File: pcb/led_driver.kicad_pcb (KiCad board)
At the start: 2 copper layers, 99.8 x 73.5 mm, 60 parts, among them J1 48V IN, J2 LED, J3 12V IN, J4 INTERLOCK, Q1 IRF540N, SW3 ARM, U1 TC4427xOA, U2 74HC74, U3 74HC08, U4 LM393

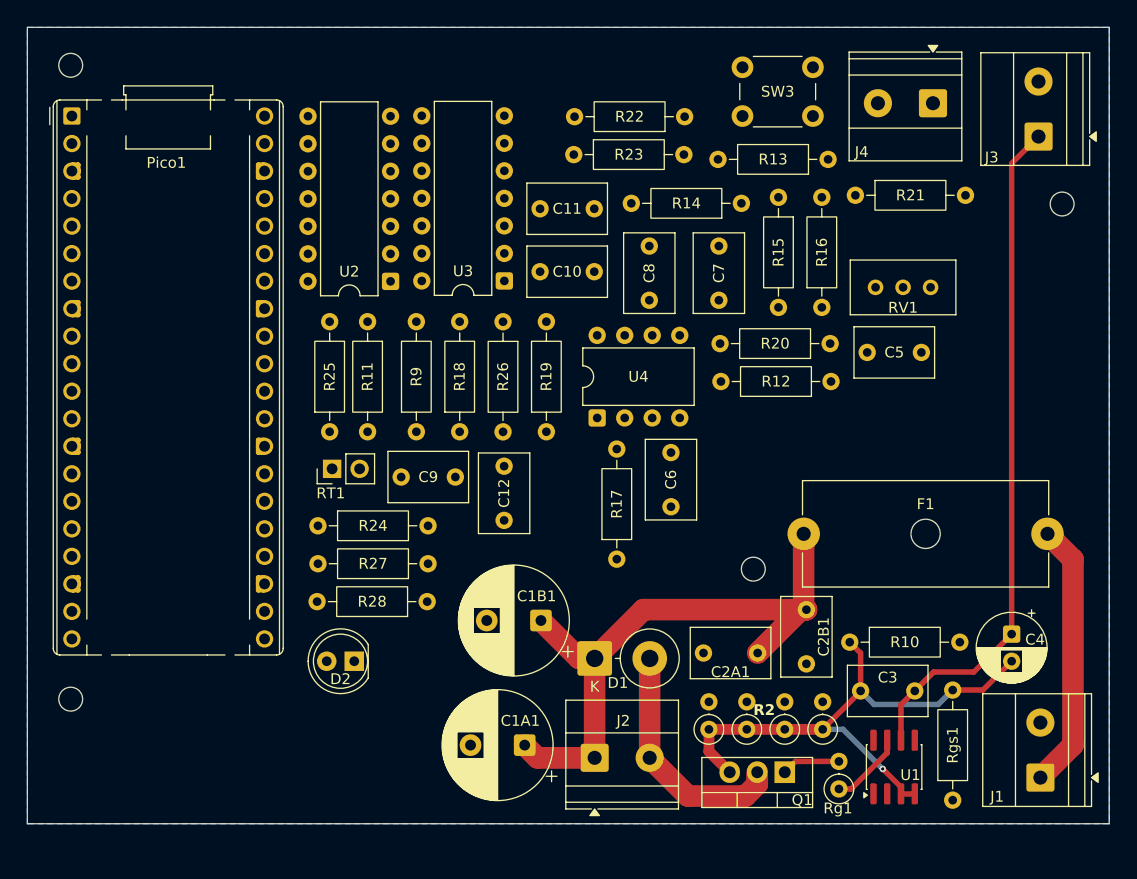
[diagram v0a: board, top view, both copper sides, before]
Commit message: Initial routing for LED driver
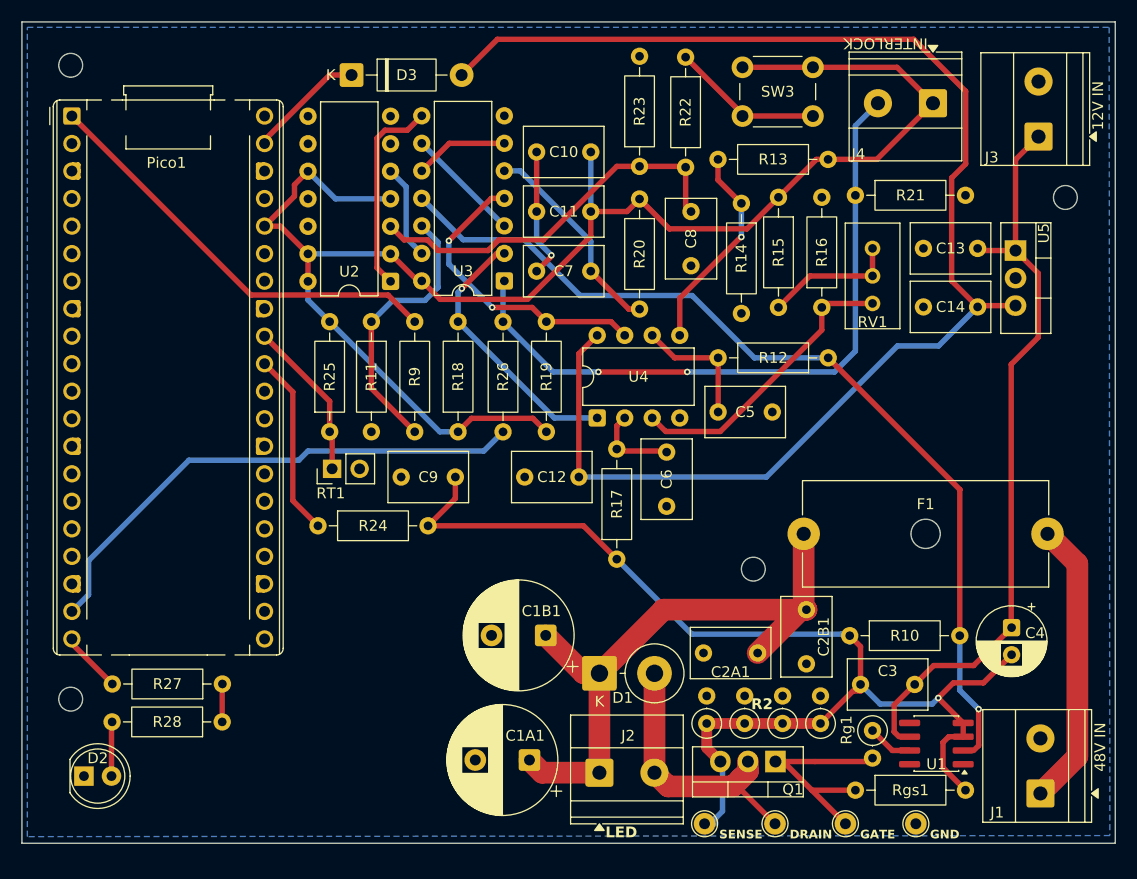
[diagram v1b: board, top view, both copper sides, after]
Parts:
- added C13: 100nF, Capacitor_THT:C_Rect_L7.2mm_W4.5mm_P5.00mm_FKS2_FKP2_MKS2_MKP2, F.Cu at (184.2, 80.4)
- added C14: 100nF, Capacitor_THT:C_Rect_L7.2mm_W4.5mm_P5.00mm_FKS2_FKP2_MKS2_MKP2, F.Cu at (179.2, 85.8)
- added D3: 1N5819, Diode_THT:D_DO-41_SOD81_P10.16mm_Horizontal, F.Cu at (126.4, 64.4)
- added TP1: TestPoint, TestPoint:TestPoint_THTPad_D2.0mm_Drill1.0mm, F.Cu at (172.0, 133.5)
- added TP2: TestPoint, TestPoint:TestPoint_THTPad_D2.0mm_Drill1.0mm, F.Cu at (165.5, 133.5)
- added TP3: TestPoint, TestPoint:TestPoint_THTPad_D2.0mm_Drill1.0mm, F.Cu at (159.0, 133.5)
- added TP4: TestPoint, TestPoint:TestPoint_THTPad_D2.0mm_Drill1.0mm, F.Cu at (178.5, 133.5)
- added U5: L7805, Package_TO_SOT_THT:TO-220-3_Vertical, F.Cu at (187.7, 80.6)
- moved D2 27.1 mm to (101.7, 129.1), turned to 0 degrees
- moved R20 22.1 mm to (153.0, 75.8), turned to -90 degrees
- moved R27 22.0 mm to (114.5, 120.6)
- moved R28 21.9 mm to (114.5, 124.1)
- moved C5 14.8 mm to (160.2, 95.5)
- moved C7 12.1 mm to (148.5, 82.5), turned to 180 degrees
- moved C10 11.1 mm to (148.5, 71.5)
- moved Rgs1 9.03 mm to (172.9, 130.4), turned to 0 degrees
- moved C12 6.97 mm to (147.4, 101.5), turned to 180 degrees
- moved RV1 6.45 mm to (174.5, 80.4), turned to 90 degrees
- moved Rg1 6.22 mm to (174.5, 124.9), turned to -90 degrees
- moved R23 6.17 mm to (153.0, 72.8), turned to 90 degrees
- moved R22 5.49 mm to (157.2, 62.8), turned to -90 degrees
- moved C8 5.00 mm to (157.8, 77.0)
- moved U1 4.46 mm to (180.4, 126.1), turned to 180 degrees
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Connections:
- net Net-(J1-Pin_1) renamed /+48V
- net Net-(J3-Pin_1) renamed +12V
- Pico1 pad 39: +5V -> Net-(D3-K)
- Pico1 pad 40: +5V -> unconnected-(Pico1-VBUS-Pad40)
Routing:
- net +3V3: track 0.00 -> 148.1 mm
- net +5V: track 0.00 -> 131.9 mm
- net PWM_GATED: track 0.00 -> 85.8 mm, vias 0 -> 1
- net IL_OK: track 0.00 -> 62.9 mm, vias 0 -> 2
- net SENSE: track 52.6 -> 107.3 mm
- net Net-(Pico1-GPIO14): track 0.00 -> 48.5 mm
- net Net-(Pico1-GPIO0): track 0.00 -> 39.5 mm
- net ARM: track 0.00 -> 35.7 mm
- net DUTY_OK: track 0.00 -> 27.8 mm, vias 0 -> 2
- net REF_I: track 0.00 -> 27.0 mm
- net PWM_IN: track 0.00 -> 25.6 mm
- net OC_OK: track 0.00 -> 25.0 mm, vias 0 -> 1
- net REF_D: track 0.00 -> 19.5 mm, vias 0 -> 1
- net POR_OK: track 0.00 -> 19.4 mm
- net CLR_N: track 0.00 -> 18.7 mm
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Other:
- board size 99.8 x 73.5 mm -> 100.9 x 75.8 mm
- board text added: "12V IN"
- board text added: "48V IN"
- board text added: "DRAIN"
- board text added: "GATE"
- board text added: "GND"
- board text added: "INTERLOCK"
- board text added: "LED"
- board text added: "SENSE"

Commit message: Fix some constraint error and violations
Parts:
- added R29: 10k, Resistor_THT:R_Axial_DIN0207_L6.3mm_D2.5mm_P10.16mm_Horizontal, F.Cu at (168.2, 94.5)
- Q1: value IRF540N -> STP30NF10
- R13: value 1k -> 10k
- R14: value 9.1k -> 8.2k
- Rgs1: footprint Resistor_THT:R_Axial_DIN0207_L6.3mm_D2.5mm_P10.16mm_Horizontal -> Resistor_THT:R_Axial_DIN0207_L6.3mm_D2.5mm_P2.54mm_Vertical
- U1: value TC4427xOA -> MIC4427
- moved D2 19.9 mm to (120.5, 122.5), turned to 180 degrees
- moved R27 10.0 mm to (104.5, 120.8), turned to 0 degrees
- moved R28 9.98 mm to (104.5, 124.2), turned to 0 degrees
- moved Rgs1 2.57 mm to (170.4, 129.8), turned to 90 degrees
- moved Rg1 0.53 mm to (174.0, 124.9)
- moved R14 0.52 mm to (162.4, 75.7)
- moved R16 0.22 mm to (169.6, 85.8)
- moved R15 0.18 mm to (166.0, 75.7)
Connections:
- C3 pad 2: SENSE -> GND
- C4 pad 2: SENSE -> GND
- R10 pad 1: SENSE -> GND
- U1 pad 3: SENSE -> GND
- U1 pad 4: SENSE -> GND
- U2 pad 5: Net-(U2A-Q) -> Q
- U3 pad 13: Net-(U2A-Q) -> Q
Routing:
- net SENSE: track 107.3 -> 66.9 mm, vias 1 -> 0
- net Net-(Pico1-GPIO15): track 5.70 -> 16.3 mm
- net DUTY_AVG: track 11.9 -> 20.7 mm
- net Net-(U2A-Q): track 8.77 -> 0.00 mm
- net Q: track 3.51 -> 12.3 mm
- net Net-(Q1-G): track 22.0 -> 19.1 mm
- net GND: track 12.1 -> 14.4 mm, vias 1 -> 2
- net DUTY_OK: track 27.8 -> 29.3 mm
- net Net-(D2-A): track 5.02 -> 4.06 mm
- net REF_D: track 19.5 -> 19.0 mm
- net Net-(U1-OUT_A): track 4.18 -> 4.69 mm
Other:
- board text added: "Fast-Switching LED Driver"
- board text added: "by Joshua Lam"

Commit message: First revision
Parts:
- moved H1 24.1 mm to (175.2, 131.1)
- moved C9 13.0 mm to (123.7, 105.7), turned to 0 degrees
- moved R24 7.76 mm to (129.6, 101.4)
- moved RT1 0.84 mm to (124.0, 101.2)
- moved R25 0.10 mm to (124.3, 97.3)
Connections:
- C9 pad 1: SENSE -> Net-(Pico1-GPIO26_ADC0)
- Pico1 pad 33: unconnected-(Pico1-AGND-Pad33) -> GND
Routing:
- net Q: track 12.3 -> 73.3 mm, vias 0 -> 2
- net SENSE: track 66.9 -> 57.0 mm
- net Net-(Pico1-GPIO26_ADC0): track 17.0 -> 24.5 mm
- net Net-(Pico1-GPIO27_ADC1): track 14.8 -> 15.7 mm
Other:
- board size 100.9 x 75.8 mm -> 100 x 75.3 mm
- board text added: "Rev 1.0 - 20261010"
- board text added: "TAPE HERE"
- board text added: "WEAR EYE PROTECTION WHEN OPERATING"
- board text added: "by Joshua Lam me@joshlam.dev"
- board text added: "◂"
- board text removed: "by Joshua Lam"
